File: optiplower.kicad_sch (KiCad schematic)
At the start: 19 parts, among them J1 Conn_01x02, J2 Conn_01x03, U1 LR7533-M, U2 XL4015, U3 DS2502, U4 ATtiny25-20SS, U5 ATtiny85-20P

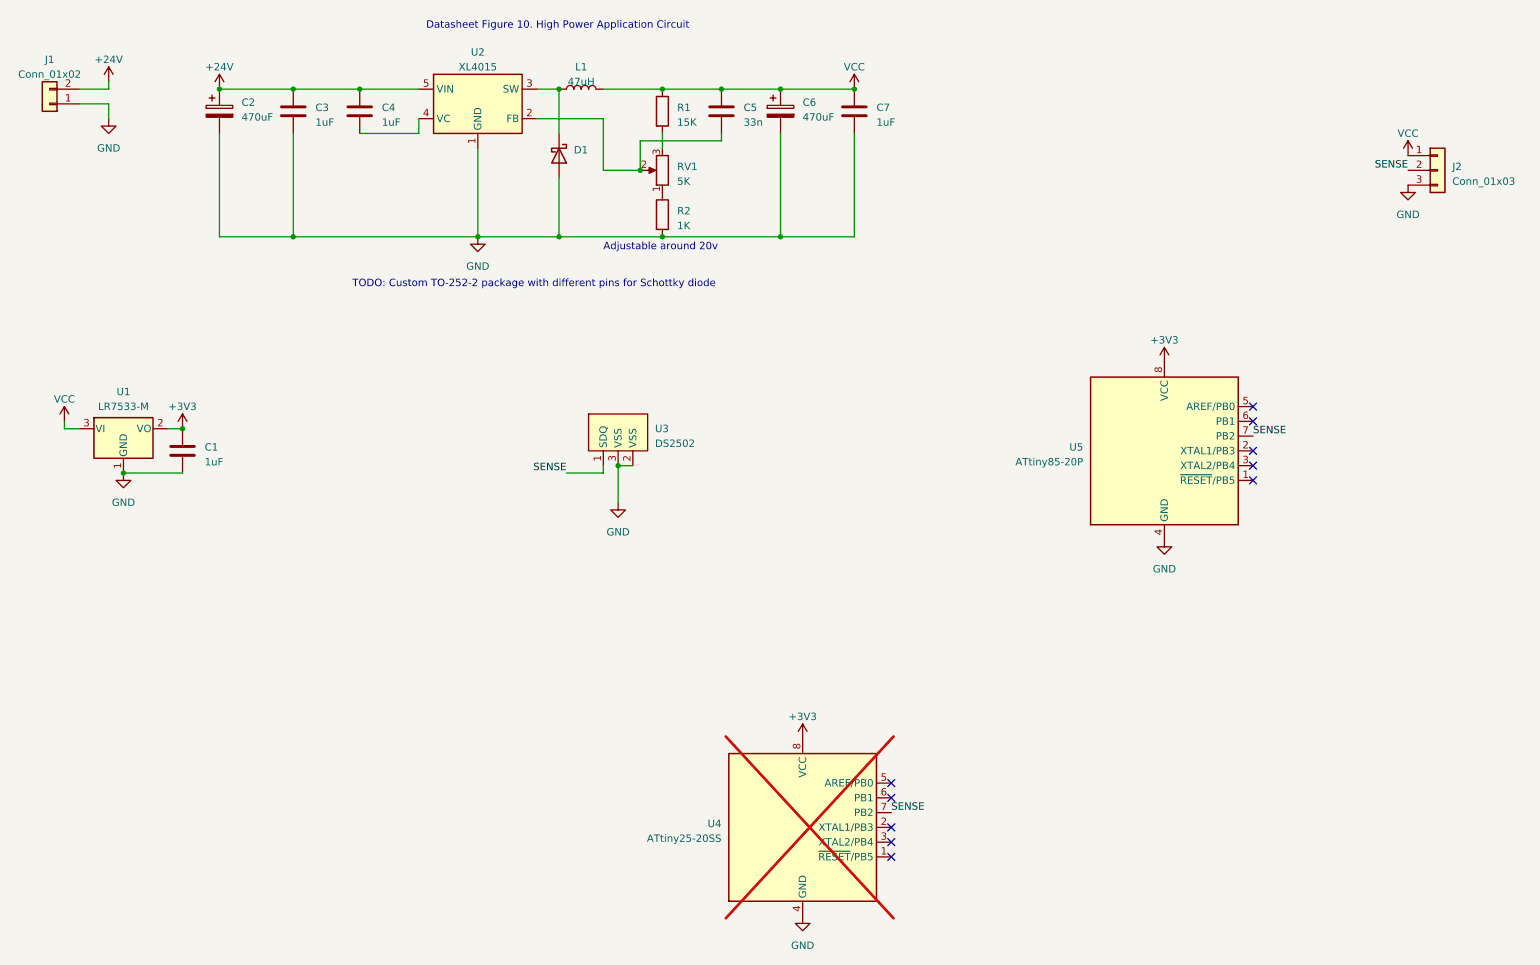
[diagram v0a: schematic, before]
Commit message: V3 with upside down regulator
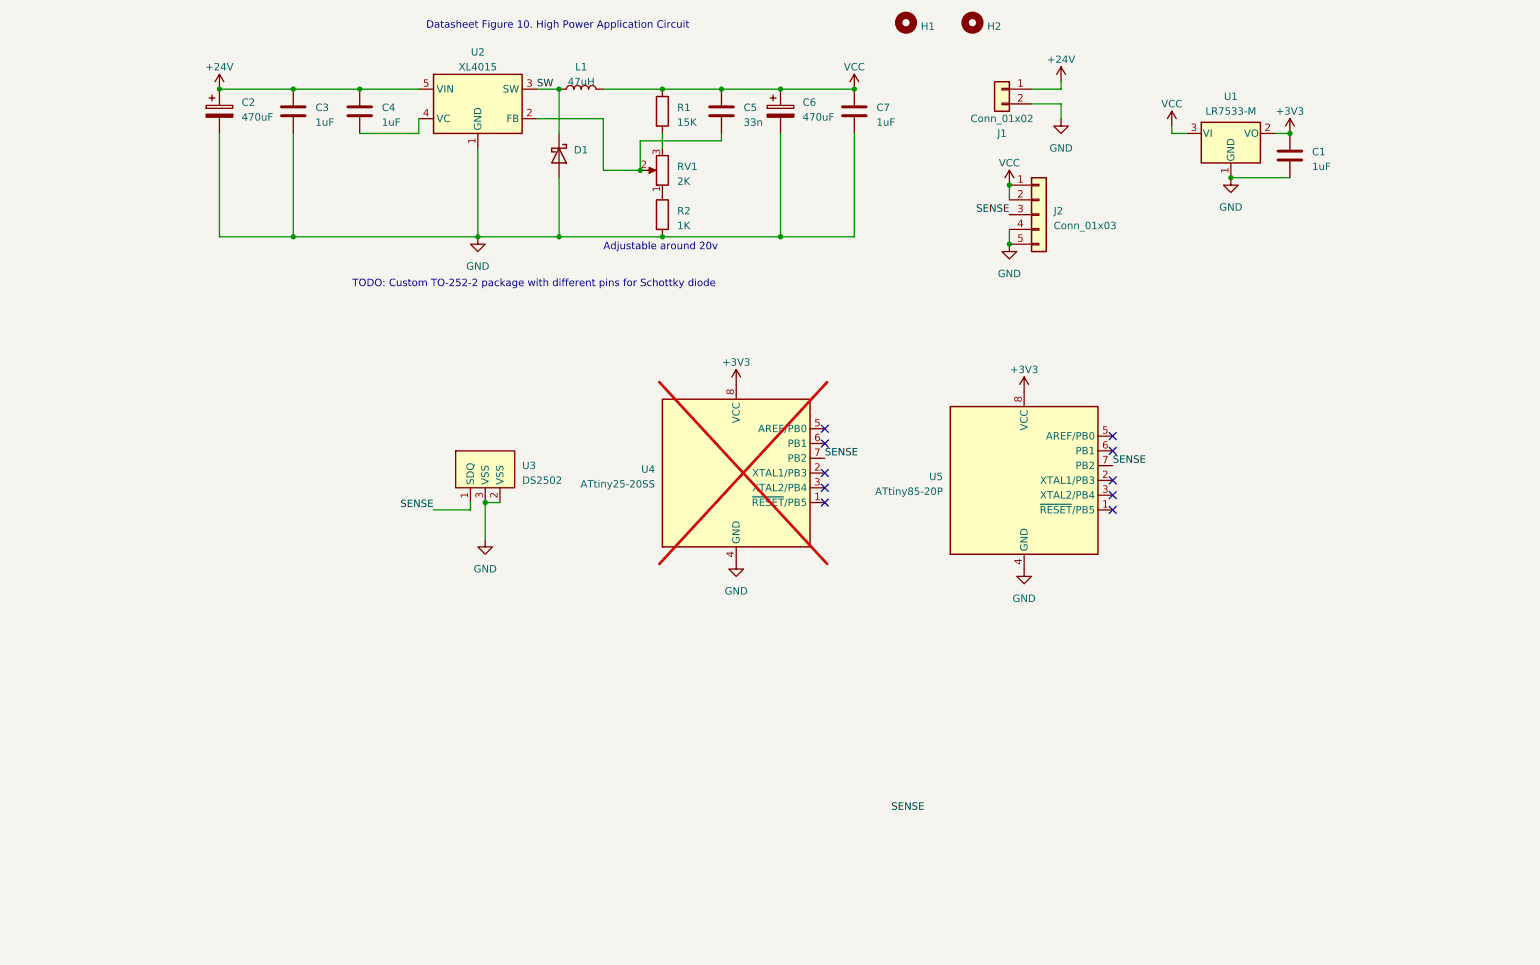
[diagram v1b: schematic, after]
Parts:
- added H1, H2: ~, MountingHole:MountingHole_2.2mm_M2, symbol Mechanical:MountingHole
- C2, C6: footprint Capacitor_SMD:CP_Elec_10x10.5 -> Optiplower:CP_Radial_D8.0mm_P3.50mm_H11.5; LCSC (none) -> C88730
- J1: footprint Connector_Wire:SolderWire-0.5sqmm_1x02_P4.8mm_D0.9mm_OD2.3mm -> Optiplower:5.08_PWR_IN
- J2: footprint Connector_Wire:SolderWire-0.5sqmm_1x03_P4.8mm_D0.9mm_OD2.3mm -> Connector_PinHeader_1.27mm:PinHeader_1x05_P1.27mm_Vertical; symbol Connector_Generic:Conn_01x03 -> Connector_Generic:Conn_01x05; now left out of the parts list
- L1: footprint (none) -> Optiplower:L_MDA1050_10x11mm
- RV1: value 5K -> 2K; footprint Resistor_SMD:R_0805_2012Metric_Pad1.20x1.40mm_HandSolder -> Potentiometer_SMD:Potentiometer_Bourns_3314G_Vertical; LCSC (none) -> C711704
- U3: footprint Package_TO_SOT_THT:TO-92L_Inline -> Package_TO_SOT_THT:TO-92_Inline
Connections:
- net +24V: now also J1.1 (Pin_1); no longer J1.2 (Pin_2)
- net GND: now also J1.2 (Pin_2), J2.4 (Pin_4), J2.5 (Pin_5); no longer J1.1 (Pin_1), J2.3 (Pin_3)
- net SENSE: now also J2.3 (Pin_3); no longer J2.2 (Pin_2)
- net VCC: now also J2.2 (Pin_2)
- net SW: now reaches D1.1 (K), L1.1, U2.3 (SW)
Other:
- moved on the sheet: C1, J1, U1, U3, U4, U5

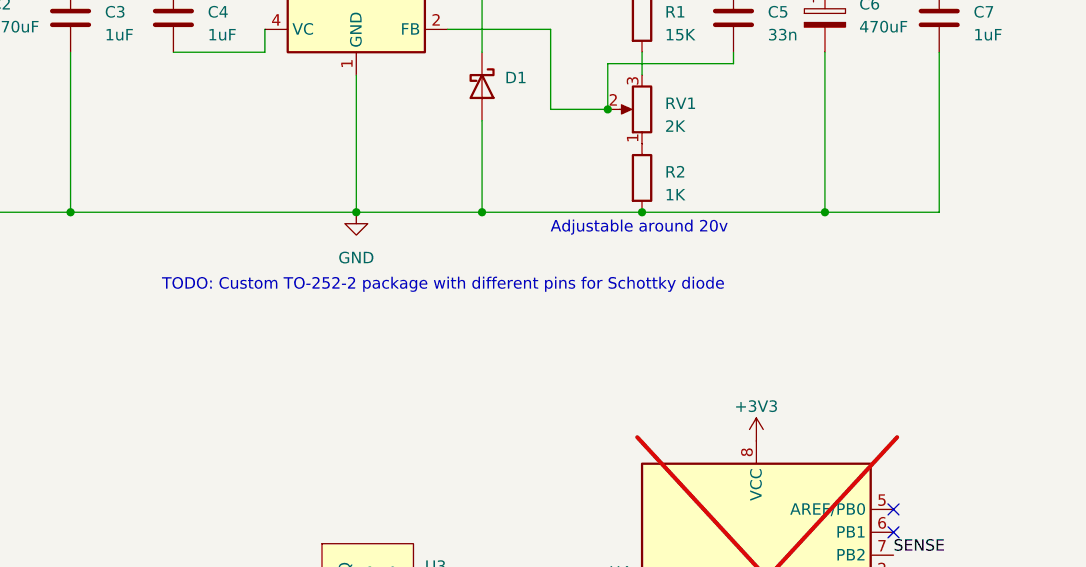
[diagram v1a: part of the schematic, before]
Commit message: Add LMR14050 part
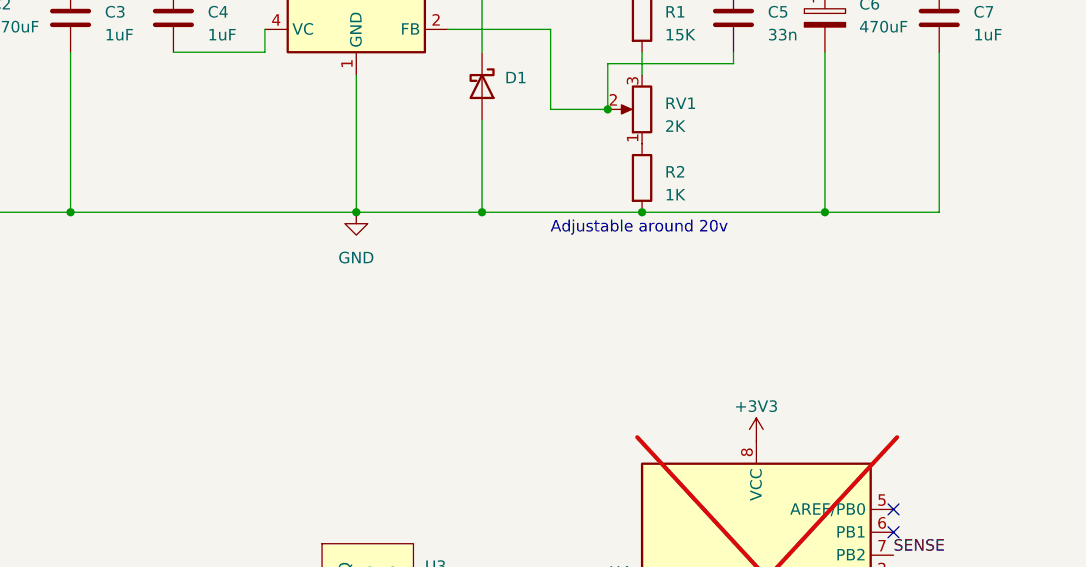
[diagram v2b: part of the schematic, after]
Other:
- note removed: "TODO: Custom TO-252-2 package with different pins for Schottky diode"
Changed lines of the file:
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@@
-    (effects (font (size 1.27 1.27)) (justify left bottom))
-  )
-  (text "TODO: Custom TO-252-2 package with different pins for Schottky diode"
-    (at 76.2 66.04 0)
     (effects (font (size 1.27 1.27)) (justify left bottom))
   )

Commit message: Stuff
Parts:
- added U6: DS2502S+, Package_TO_SOT_SMD:SOT-23, symbol Optiplower:DS2502
- C1, C3, C4, C7: LCSC (none) -> C28323; SmartMatch (none) -> 1uF X7R 0805
- C2, C6: MPN (none) -> 25PX470MEFC8X11.5; Manufacturer (none) -> Rubycon
- C5: LCSC (none) -> C159777; SmartMatch (none) -> 33n X7R 0805
- D1: value MBRD1045 -> SK84B; footprint Optiplower:TO-252-2 -> Diode_SMD:D_SMB_Handsoldering; LCSC C5137764 -> C65016; MPN (none) -> SK84B; Manufacturer (none) -> MDD
- J1, U3, U5: now not fitted; now left out of the parts list
- L1: Current 12A -> (none); LCSC (none) -> C2847567; MPN (none) -> MDA1050-470M; Manufacturer (none) -> Koher
- R1: value 15K -> 150K; LCSC (none) -> C114558; SmartMatch (none) -> 150K 0805 1%
- R2: value 1K -> 10K; LCSC (none) -> C140868; SmartMatch (none) -> 10K 0805 1%
- RV1: value 2K -> 1K; footprint Potentiometer_SMD:Potentiometer_Bourns_3314G_Vertical -> Potentiometer_SMD:Potentiometer_Bourns_TC33X_Vertical; LCSC C711704 -> C719174; MPN (none) -> TC33X-2-102E; Manufacturer (none) -> Bourns
- U1: MPN (none) -> LR7533-M; Manufacturer (none) -> LR
- U2: MPN (none) -> XL4015E1; Manufacturer (none) -> XLSEMI
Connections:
- net GND: now also J2.1 (Pin_1), U6.2 (VSS), U6.3 (VSS); no longer J2.4 (Pin_4)
- net SENSE: now also U6.1 (SDQ)
- net VCC: now also J2.4 (Pin_4); no longer J2.1 (Pin_1)
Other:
- note added: "Adjustability from 18.29v - 20.125v"
- note removed: "Adjustable around 20v"

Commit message: Use JLC basic parts for some things
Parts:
- C5: LCSC C159777 -> C1739
- R1: LCSC C114558 -> C17470
- R2: LCSC C140868 -> C17414
- RV1: LCSC C719174 -> C17513
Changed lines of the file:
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@@
       (effects (font (size 1.27 1.27)) hide)
     )
-    (property "LCSC" "C114558" (at 129.54 35.56 0)
+    (property "LCSC" "C17470" (at 129.54 35.56 0)
       (effects (font (size 1.27 1.27)) hide)
     )
@@
       (effects (font (size 1.27 1.27)) hide)
     )
-    (property "LCSC" "C159777" (at 139.7 35.56 0)
+    (property "LCSC" "C1739" (at 139.7 35.56 0)
       (effects (font (size 1.27 1.27)) hide)
     )
@@
       (effects (font (size 1.27 1.27)) hide)
     )
-    (property "LCSC" "C719174" (at 129.54 45.72 0)
+    (property "LCSC" "C17513" (at 129.54 45.72 0)
       (effects (font (size 1.27 1.27)) hide)
     )
@@
       (effects (font (size 1.27 1.27)) hide)
     )
-    (property "LCSC" "C140868" (at 129.54 53.34 0)
-      (effects (font (size 1.27 1.27)) hide)
-    )
+    (property "LCSC" "C17414" (at 129.54 53.34 0)
+      (effects (font (size 1.27 1.27)) hide)
+    )

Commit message: Production files
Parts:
- RV1: LCSC C17513 -> C719174
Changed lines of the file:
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@@
       (effects (font (size 1.27 1.27)) hide)
     )
-    (property "LCSC" "C17513" (at 129.54 45.72 0)
+    (property "LCSC" "C719174" (at 129.54 45.72 0)
       (effects (font (size 1.27 1.27)) hide)
     )

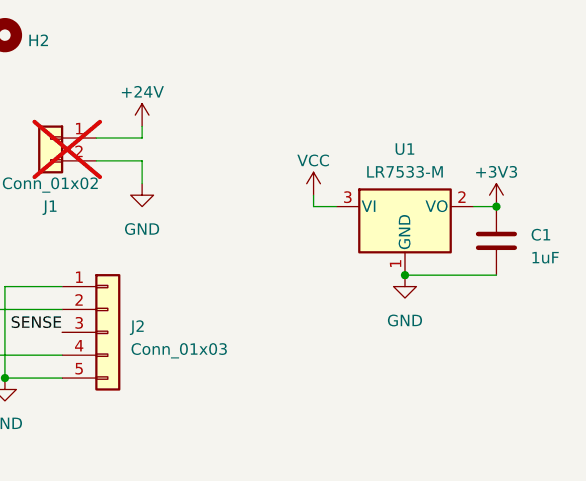
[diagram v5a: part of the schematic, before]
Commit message: Fix 3.3v regulator pinout
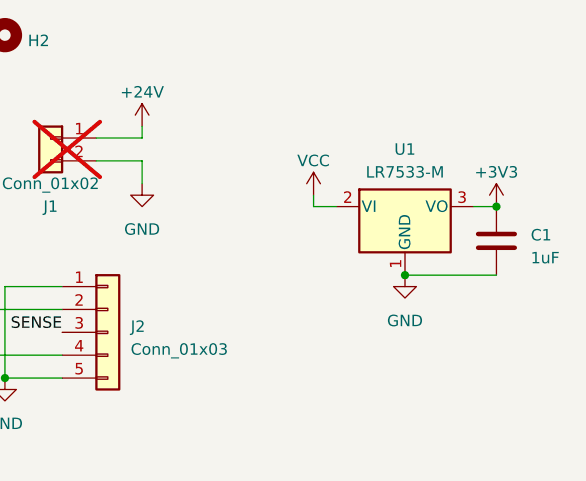
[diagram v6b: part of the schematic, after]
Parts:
- U1: symbol Regulator_Linear:AZ1117-3.3 -> Optiplower:LR7533-M
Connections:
- net +3V3: now also U1.3 (VO); no longer U1.2 (VO)
- net VCC: now also U1.2 (VI); no longer U1.3 (VI)
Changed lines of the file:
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@@
       (effects (font (size 1.27 1.27)) hide)
     )
-    (property "Datasheet" "http://www.xlsemi.net/datasheet/XL4015%20datasheet-English.pdf" (at 97.79 34.29 0)
+    (property "Datasheet" "https://www.xlsemi.com/datasheet/XL4015-EN.pdf" (at 97.79 34.29 0)
       (effects (font (size 1.27 1.27)) hide)
     )
@@
     )
   )
-  (symbol (lib_id "Regulator_Linear:AZ1117-3.3") (at 227.33 39.37 0) (unit 1)
+  (symbol (lib_id "Optiplower:LR7533-M") (at 227.33 39.37 0) (unit 1)
     (in_bom yes) (on_board yes) (dnp no) (fields_autoplaced)
     (property "Reference" "U1" (at 227.33 33.02 0)
@@
       (effects (font (size 1.27 1.27) italic) hide)
     )
-    (property "Datasheet" "" (at 227.33 39.37 0)
-      (effects (font (size 1.27 1.27)) hide)
-    )
+    (property "Datasheet" "https://datasheet.lcsc.com/lcsc/2003121111_LR-LR7533-M_C486076.pdf" (at 227.33 39.37 0)
+      (effects (font (size 1.27 1.27)) hide)
+    )
